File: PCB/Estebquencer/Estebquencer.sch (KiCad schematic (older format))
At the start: 0 parts

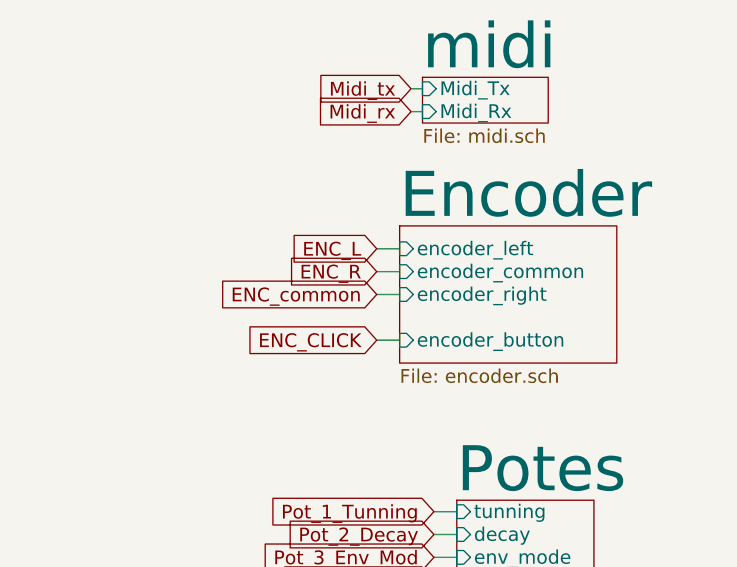
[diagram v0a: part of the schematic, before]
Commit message: se arregló cableado encoder
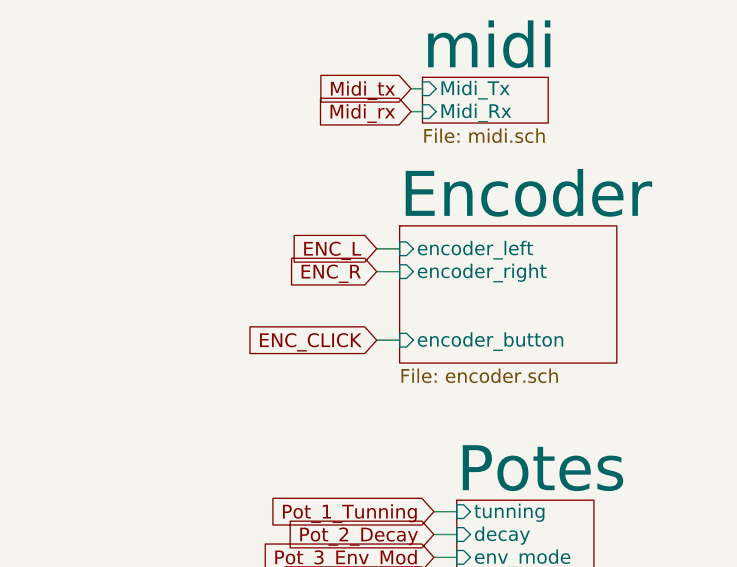
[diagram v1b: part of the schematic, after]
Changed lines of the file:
@@
 F1 "encoder.sch" 60
 F2 "encoder_left" I L 8300 4350 60
-F3 "encoder_common" I L 8300 4450 60
-F4 "encoder_right" I L 8300 4550 60
-F5 "encoder_button" I L 8300 4750 60
+F3 "encoder_right" I L 8300 4450 60
+F4 "encoder_button" I L 8300 4750 60
 $EndSheet
 Text GLabel 8200 4350 0    60   Input ~ 0
@@
 Text GLabel 8200 4750 0    60   Input ~ 0
 ENC_CLICK
-Text GLabel 8200 4550 0    60   Input ~ 0
-ENC_common
 $Sheet
 S 3450 3050 1600 900
@@
 Wire Wire Line
 	8550 5800 8450 5800
-Wire Wire Line
-	8200 4550 8300 4550
-Wire Wire Line
-	8300 4450 8200 4450
 Wire Wire Line
 	8200 4350 8300 4350
@@
 Text Notes -12650 7150 0    394  ~ 0
 ·MIDI
+Wire Wire Line
+	8200 4450 8300 4450
 $EndSCHEMATC

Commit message: se cablearon los módulos al ARM, se añadió el conector JTAG (SWD)
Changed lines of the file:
@@
 ENC_CLICK
 $Sheet
-S 3450 3050 1600 900
+S 3300 3050 900  1700
 U 5875A8C4
 F0 "ARM" 197
 F1 "arm.sch" 60
-F2 "MIDI_TX" I R 5050 3400 60
-F3 "MIDI_RX" I R 5050 3500 60
+F2 "MIDI_TX" I R 4200 3100 60
+F3 "MIDI_RX" I R 4200 3200 60
+F4 "encoder_L" I R 4200 3350 60
+F5 "encoder_R" I R 4200 3450 60
+F6 "encoder_click" I R 4200 3550 60
+F7 "DAC_Din" I R 4200 3900 60
+F8 "DAC_Sclk" I R 4200 3800 60
+F9 "DAC_#Sync" I R 4200 3700 60
+F10 "DISP_SCK" I R 4200 4150 60
+F11 "DISP_SER" I R 4200 4050 60
+F12 "DISP_EN" I R 4200 4250 60
+F13 "DISP_CHAR0" I R 4200 4350 60
+F14 "DISP_CHAR1" I R 4200 4450 60
+F15 "DISP_CHAR2" I R 4200 4550 60
+F16 "DISP_CHAR3" I R 4200 4650 60
 $EndSheet
+Text GLabel 4350 3100 2    60   Input ~ 0
+Midi_tx
+Text GLabel 4350 3200 2    60   Input ~ 0
+Midi_rx
+Text GLabel 8350 3650 0    60   Input ~ 0
+Midi_tx
+Text GLabel 8350 3750 0    60   Input ~ 0
+Midi_rx
+$Sheet
+S 8400 2300 550  700
+U 58741263
+F0 "Dac" 197
+F1 "DAC.sch" 39
+F2 "vref" I L 8400 2650 60
+F3 "vout_B" I L 8400 2950 60
+F4 "vout_A" I L 8400 2850 60
+F5 "din" I L 8400 2550 60
+F6 "sclk" I L 8400 2450 60
+F7 "#sync" I L 8400 2350 60
+$EndSheet
+Text Notes -12300 1900 0    394  ~ 0
+·Módulo Potes terminado. No tocar
+Text Notes -12300 1400 0    394  ~ 0
+·Módulo Encoder terminado. No tocar
+Text Notes -12400 4850 0    1181 ~ 0
+Falta:
+Text Notes -12500 5700 0    394  ~ 0
+·ARM
+Text Notes -12400 2600 0    394  ~ 0
+·JTAG
+Text Notes -12550 6300 0    394  ~ 0
+·MIDI
+Text GLabel 4350 3350 2    60   Input ~ 0
+ENC_L
+Text GLabel 4350 3450 2    60   Input ~ 0
+ENC_R
+Text GLabel 4350 3550 2    60   Input ~ 0
+ENC_CLICK
+Text GLabel 4350 3700 2    60   Input ~ 0
+DAC_#Sync
+Text GLabel 4350 3800 2    60   Input ~ 0
+DAC_Sclk
+Text GLabel 4350 3900 2    60   Input ~ 0
+DAC_Din
+Text GLabel 4350 4050 2    60   Input ~ 0
+DISP_SER
+Text GLabel 4350 4150 2    60   Input ~ 0
+DISP_SCK
+Text GLabel 4350 4250 2    60   Input ~ 0
+DISP_EN
+Text GLabel 4350 4350 2    60   Input ~ 0
+DISP_CHAR0
+Text GLabel 4350 4450 2    60   Input ~ 0
+DISP_CHAR1
+Text GLabel 4350 4550 2    60   Input ~ 0
+DISP_CHAR2
+Text GLabel 4350 4650 2    60   Input ~ 0
+DISP_CHAR3
 Wire Wire Line
 	8150 1000 8300 1000
@@
 Wire Wire Line
 	8300 4750 8200 4750
-Text GLabel 5150 3400 2    60   Input ~ 0
-Midi_tx
-Text GLabel 5150 3500 2    60   Input ~ 0
-Midi_rx
-Wire Wire Line
-	5150 3500 5050 3500
-Wire Wire Line
-	5050 3400 5150 3400
-Text GLabel 8350 3650 0    60   Input ~ 0
-Midi_tx
-Text GLabel 8350 3750 0    60   Input ~ 0
-Midi_rx
 Wire Wire Line
 	8400 3750 8350 3750
@@
 Wire Wire Line
 	8400 2950 8300 2950
-$Sheet
-S 8400 2300 550  700
-U 58741263
-F0 "Dac" 197
-F1 "DAC.sch" 39
-F2 "vref" I L 8400 2650 60
-F3 "vout_B" I L 8400 2950 60
-F4 "vout_A" I L 8400 2850 60
-F5 "din" I L 8400 2550 60
-F6 "sclk" I L 8400 2450 60
-F7 "#sync" I L 8400 2350 60
-$EndSheet
-Text Notes -12300 1900 0    394  ~ 0
-·Módulo Potes terminado. No tocar
-Text Notes -12300 1400 0    394  ~ 0
-·Módulo Encoder terminado. No tocar
-Text Notes -12400 4850 0    1181 ~ 0
-Falta:
-Text Notes -12500 5700 0    394  ~ 0
-·ARM
-Text Notes -12600 6400 0    394  ~ 0
-·JTAG
-Text Notes -12650 7150 0    394  ~ 0
-·MIDI
 Wire Wire Line
 	8200 4450 8300 4450
+Wire Wire Line
+	4350 3100 4200 3100
+Wire Wire Line
+	4200 3200 4350 3200
+Wire Wire Line
+	4350 3350 4200 3350
+Wire Wire Line
+	4200 3450 4350 3450
+Wire Wire Line
+	4350 3550 4200 3550
+Wire Wire Line
+	4200 3700 4350 3700
+Wire Wire Line
+	4350 3800 4200 3800
+Wire Wire Line
+	4200 3900 4350 3900
+Wire Wire Line
+	4350 4050 4200 4050
+Wire Wire Line
+	4200 4150 4350 4150
+Wire Wire Line
+	4350 4250 4200 4250
+Wire Wire Line
+	4200 4350 4350 4350
+Wire Wire Line
+	4350 4450 4200 4450
+Wire Wire Line
+	4200 4550 4350 4550
+Wire Wire Line
+	4350 4650 4200 4650
 $EndSCHEMATC

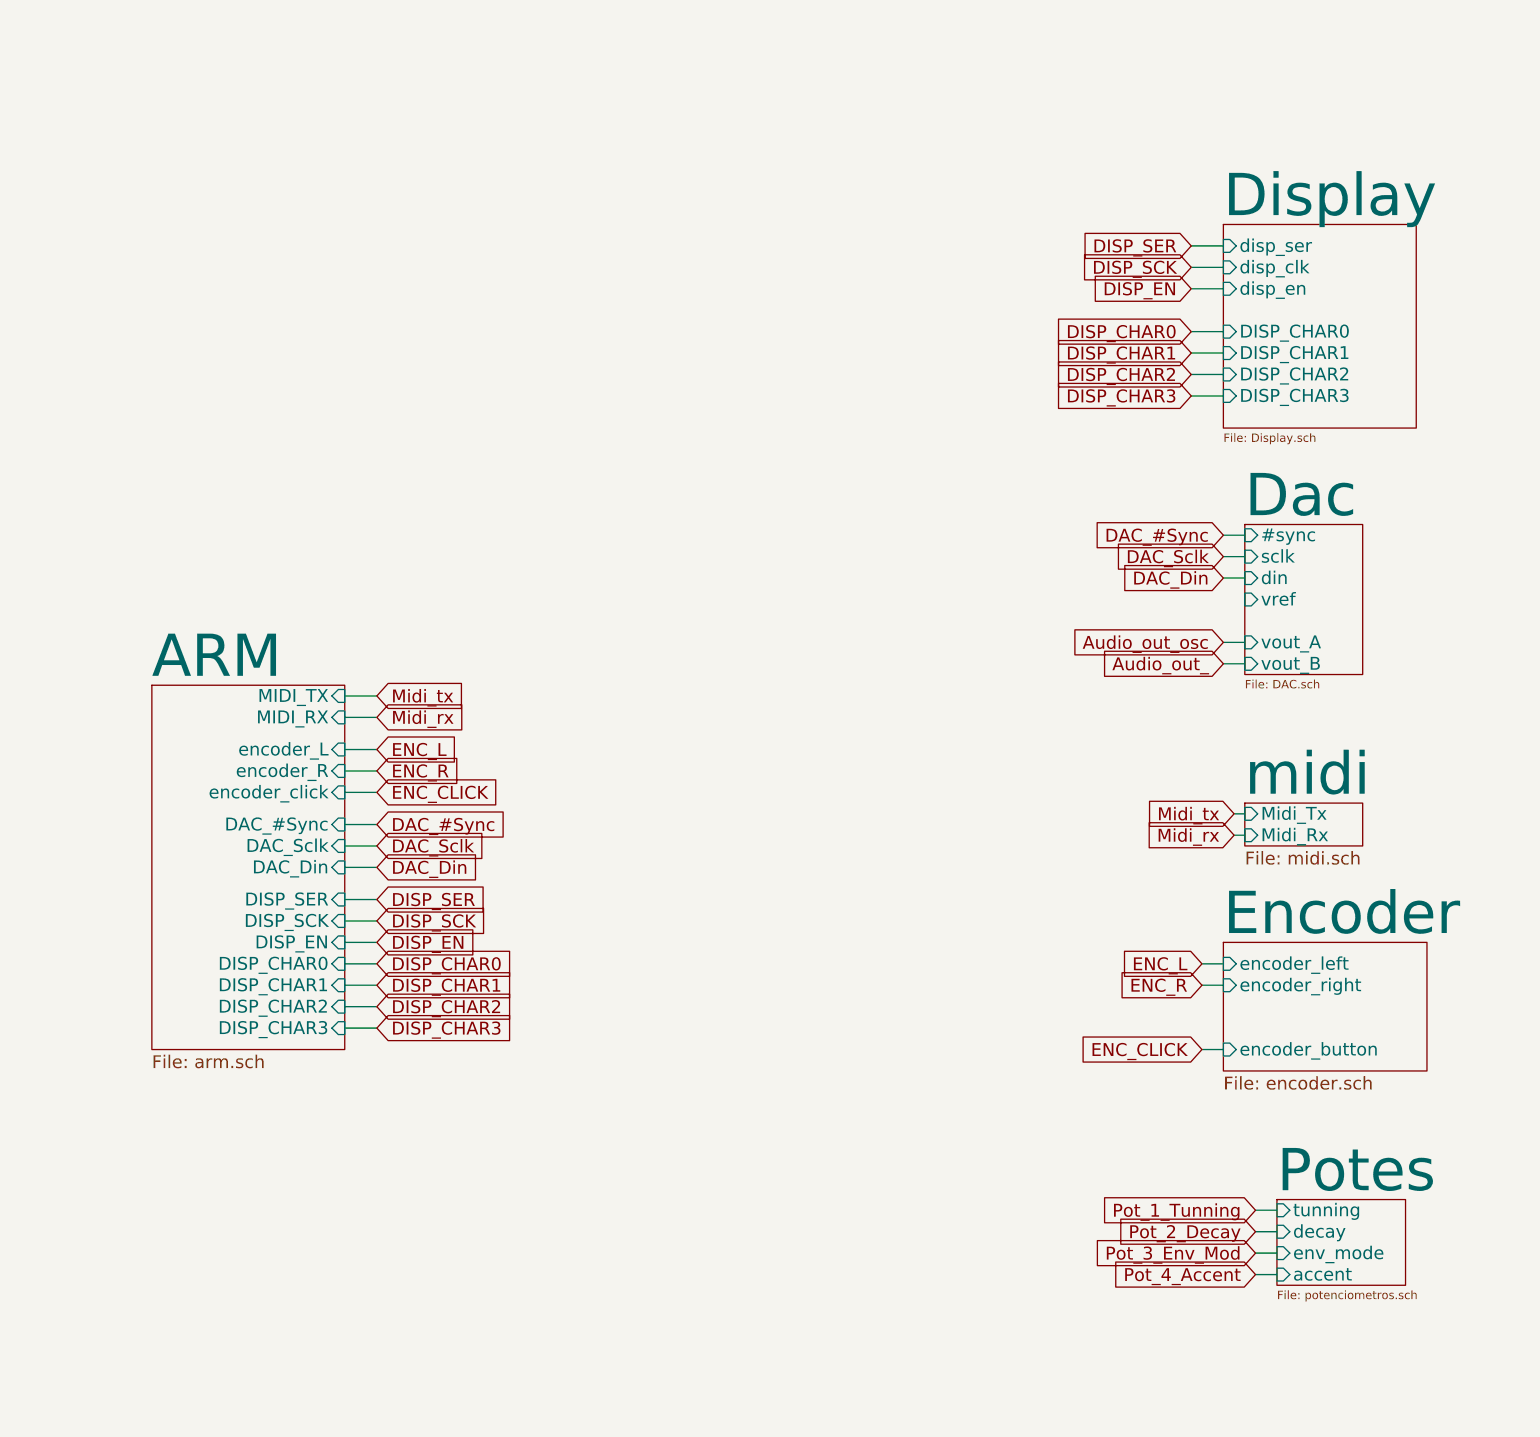
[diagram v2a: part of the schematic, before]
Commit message: Añadido proyecto ST, configuración superficial de todos los periféricos, falta crear los threads en FreeRTOS
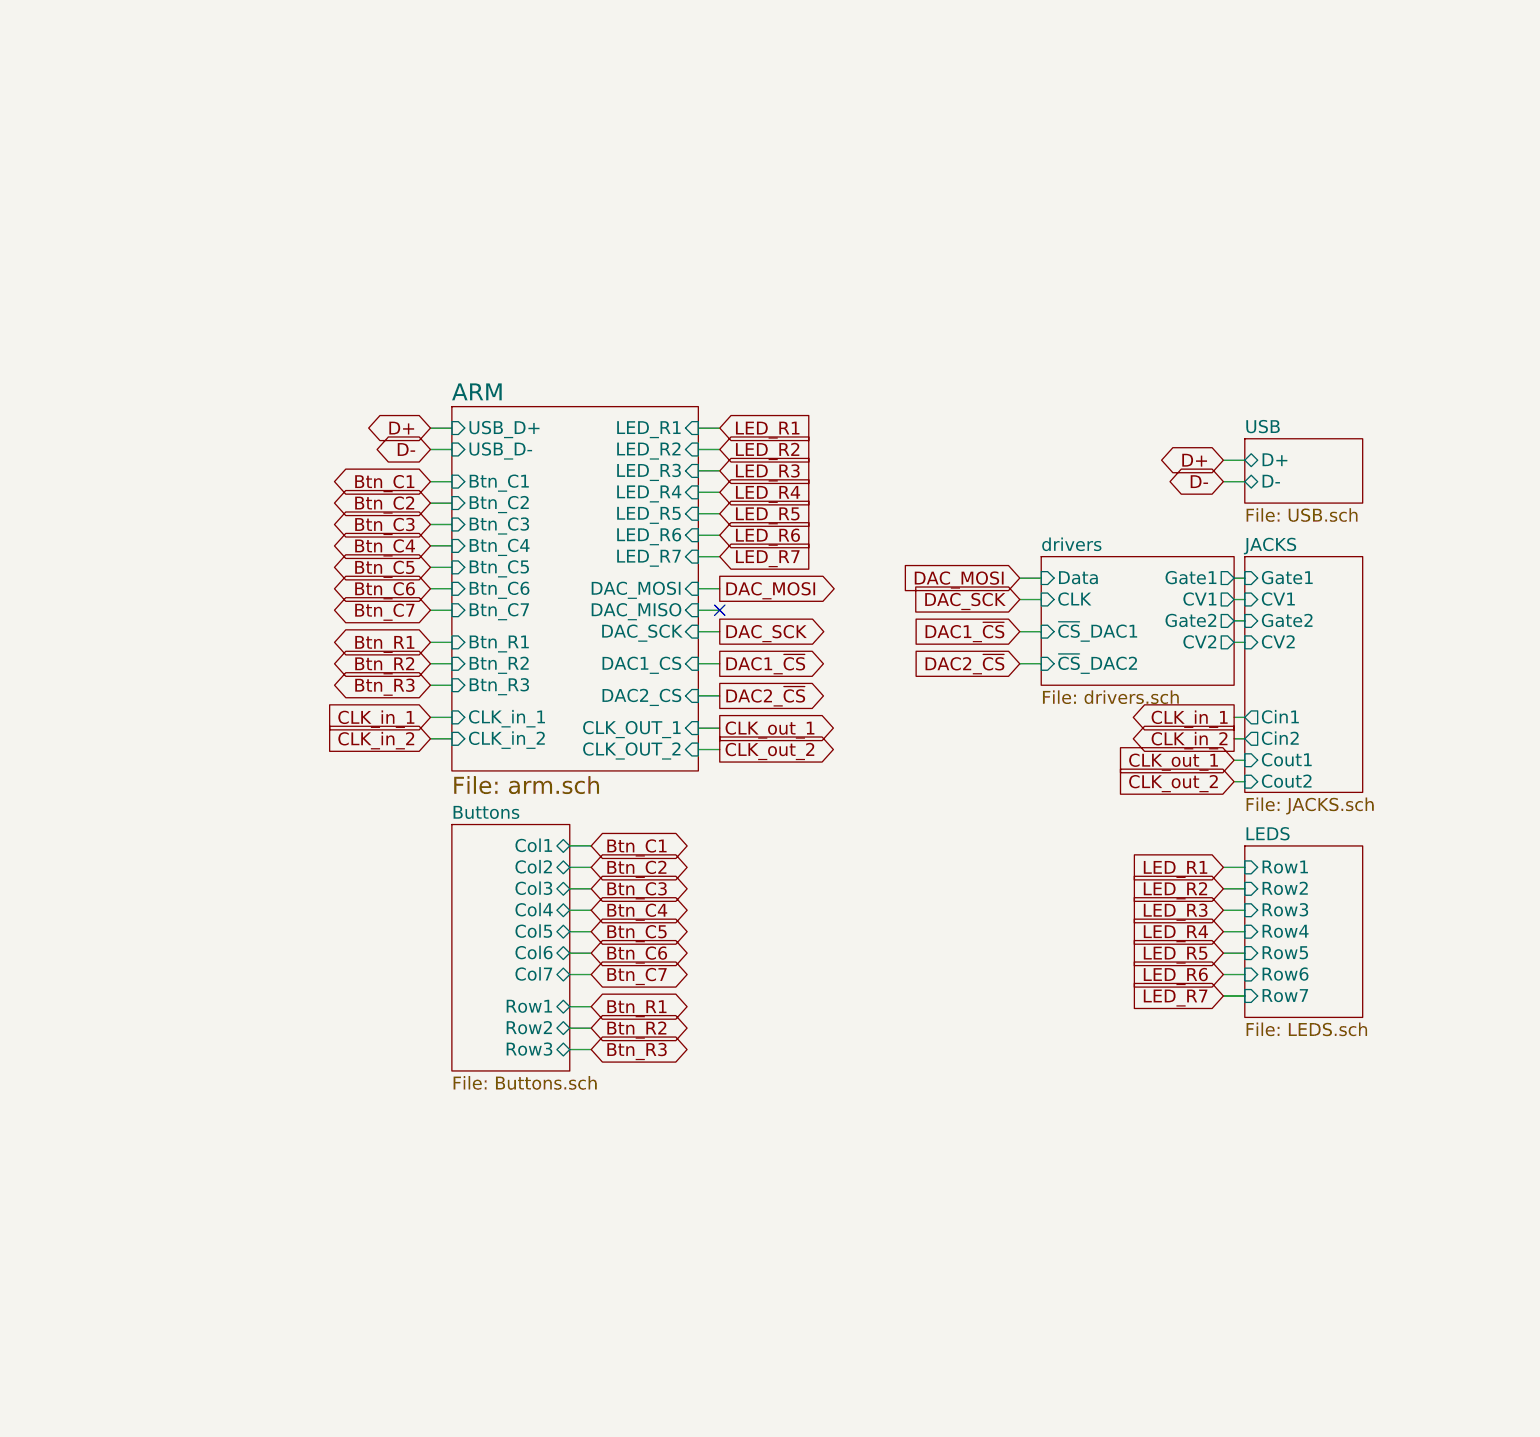
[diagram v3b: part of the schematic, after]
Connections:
- no-connect marks 0 -> 1

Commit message: Terminado módulo DAC
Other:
- note removed: "Falta:"
- note removed: "Notas:"
- note removed: "·ARM"
- note removed: "·JTAG"
- note removed: "·MIDI"
- note removed: "·Módulo DAC terminado. No tocar"
- note removed: "·Módulo Encoder terminado. No tocar"
- note removed: "·Módulo Potes terminado. No tocar"
- note removed: "·Módulo display terminado. No tocar"

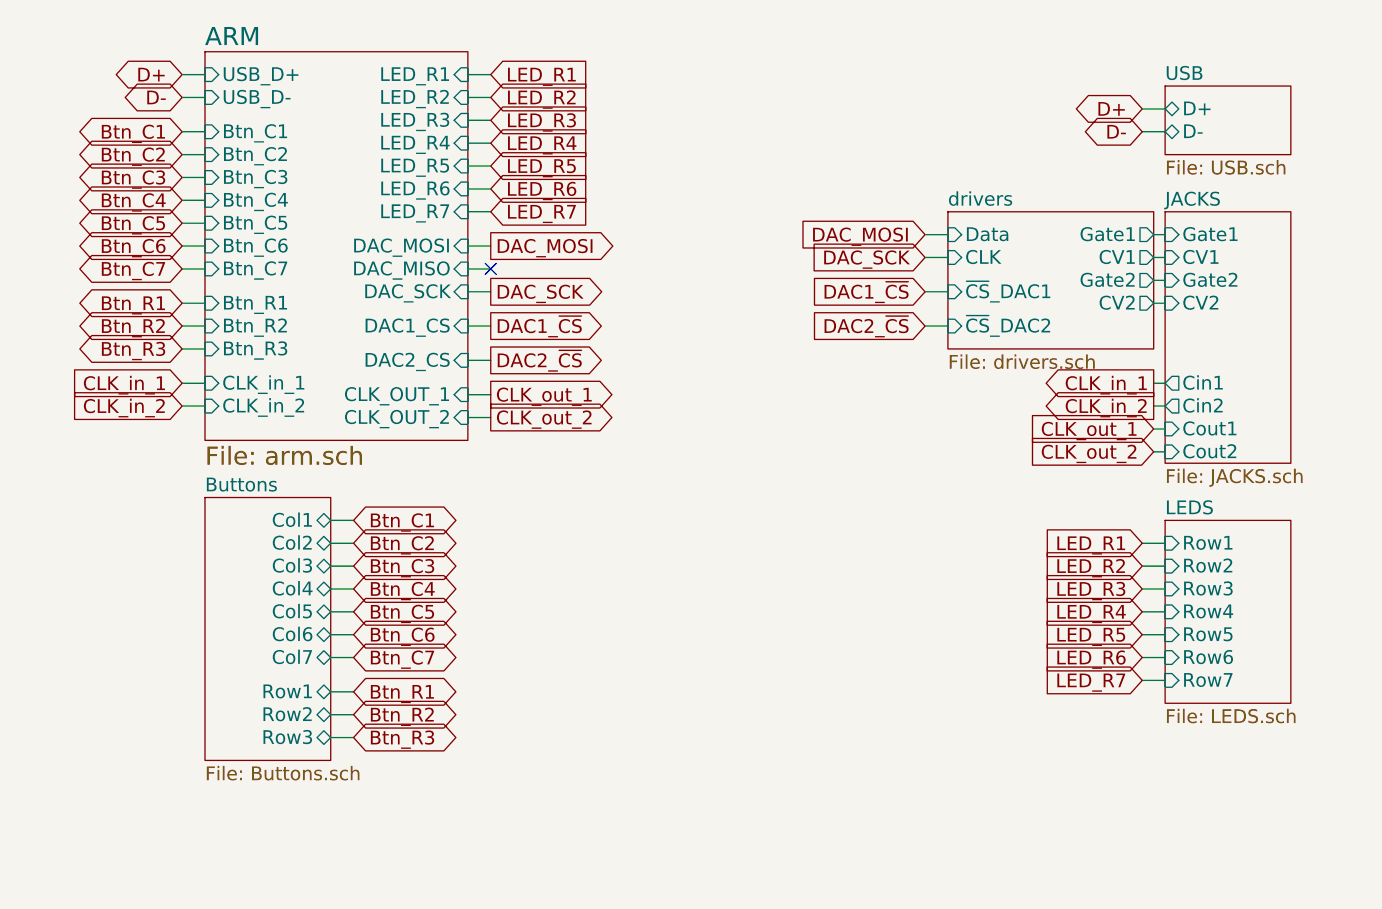
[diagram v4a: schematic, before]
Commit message: Se tuvo que cambiar el sistema de gestión de los LED y pulsadores. Con el charlieplexing no tenía los resultados esperados, así que se le añadió un HT16K33 para hacer las cosas más simples y fluídas. También se usará el mismo IC para la gestión de botones, ya que da opción.
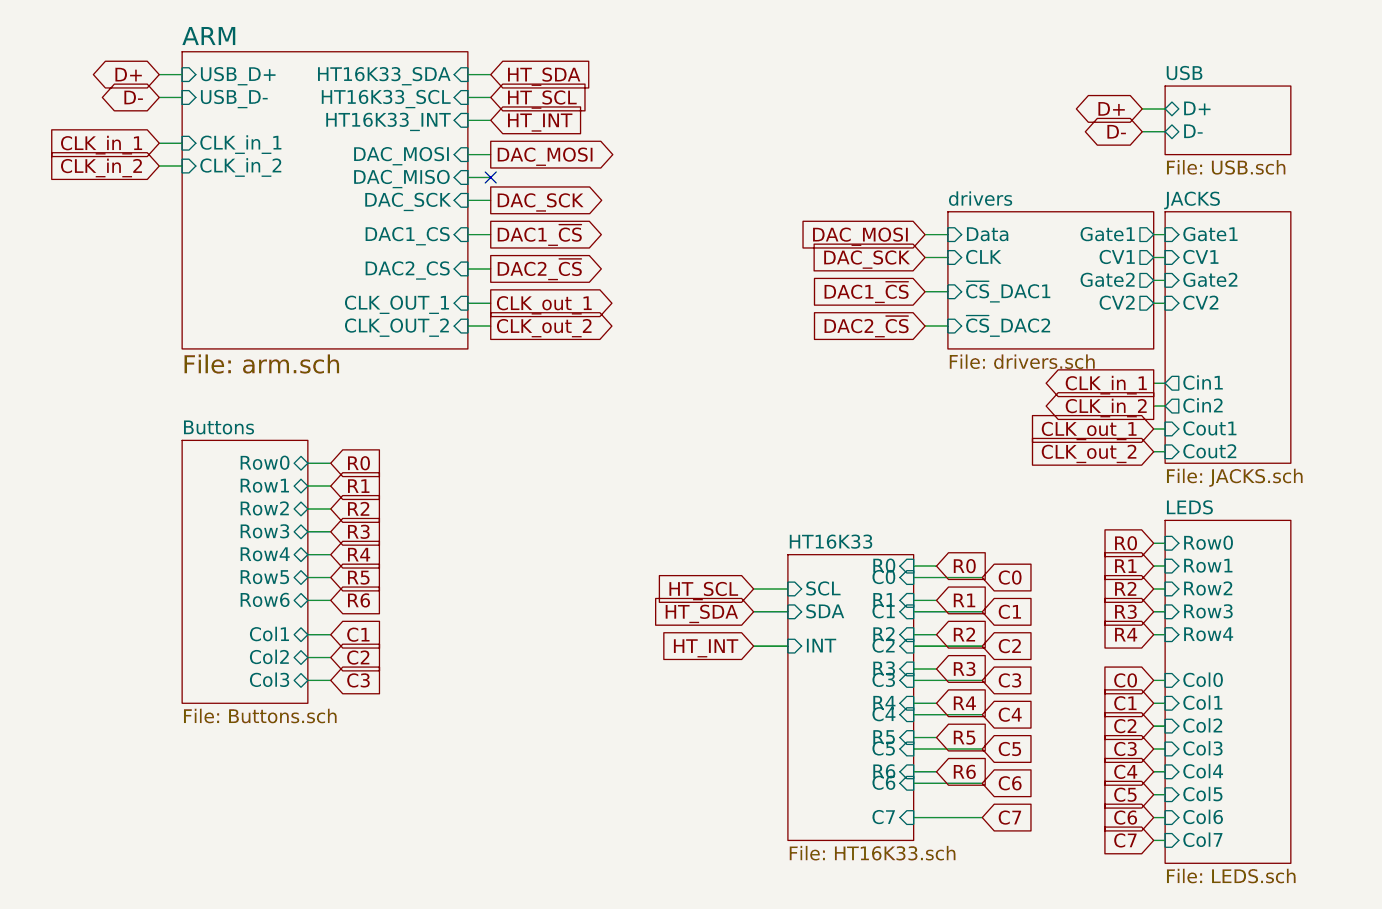
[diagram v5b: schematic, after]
